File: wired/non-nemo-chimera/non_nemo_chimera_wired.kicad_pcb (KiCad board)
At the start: 2 copper layers, 273.7 x 107 mm, 94 parts, among them X1 5.5mm, X10 5.5mm, X2 5.5mm, X3 5.5mm, X4 5.5mm, X5 5.5mm, X6 5.5mm, X7 5.5mm, X8 5.5mm, X9 5.5mm

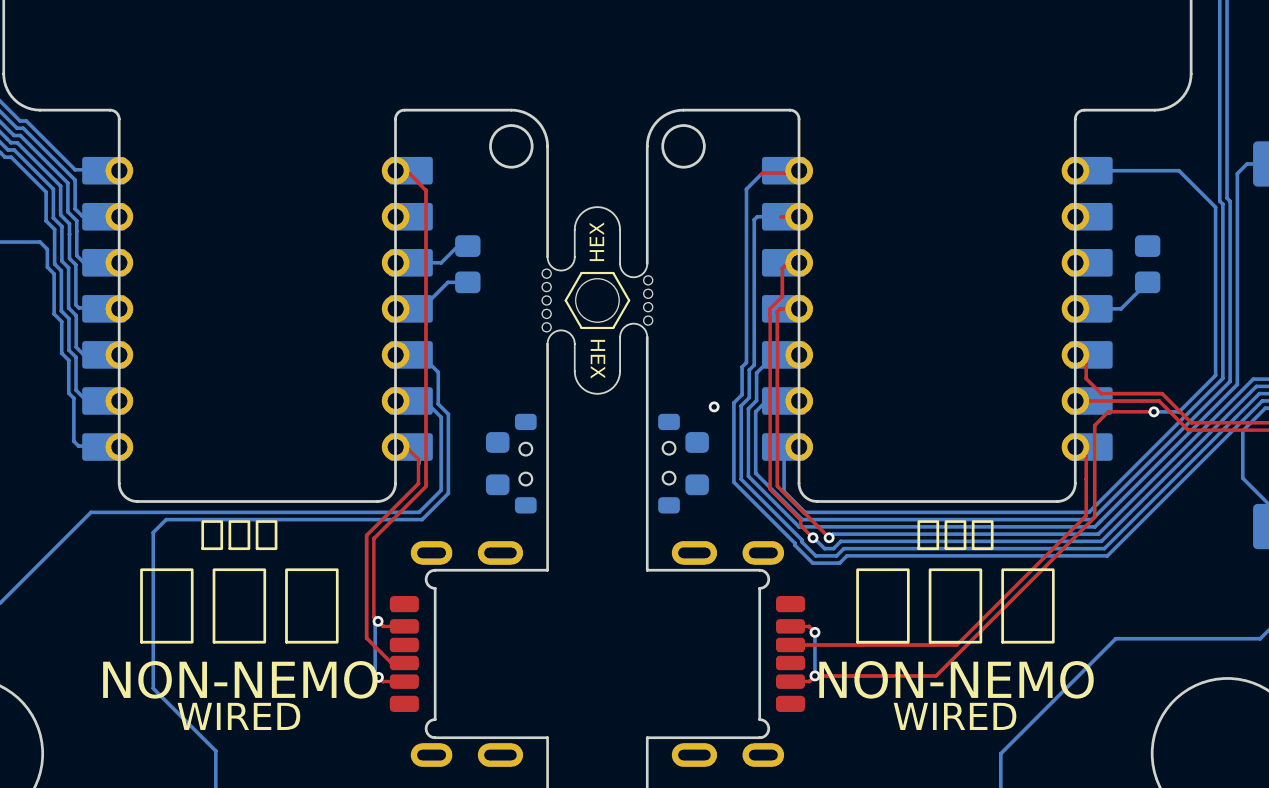
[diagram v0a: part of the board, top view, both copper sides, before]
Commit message: Chimera Wired + Case (#10)
* Updated cases for Chimera Wired

* updated README.md for Chimera Wired

* updated github workflow
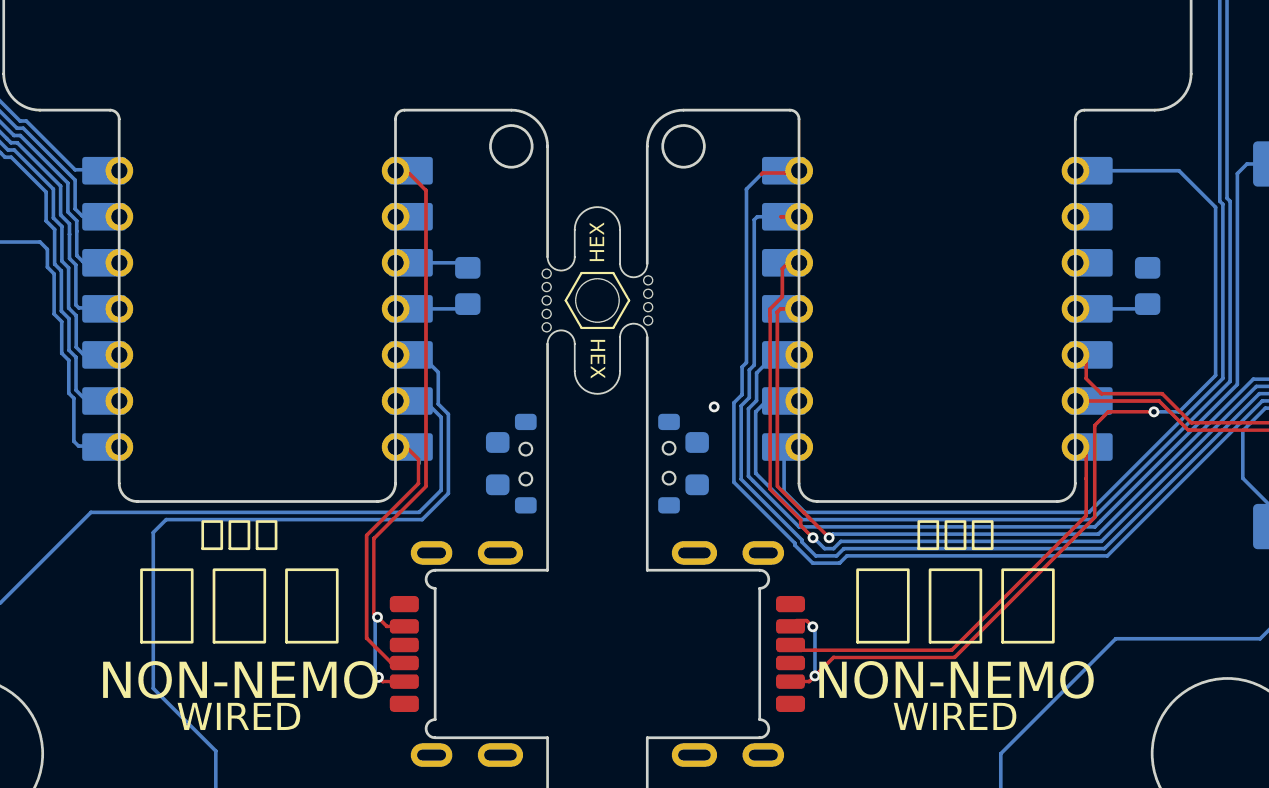
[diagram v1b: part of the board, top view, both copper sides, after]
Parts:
- moved R1 1.20 mm to (147.6, 84.2)
- moved R2 1.20 mm to (185.1, 84.2)
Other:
- board text added: "Non Nemo 0.2.1"
- board text removed: "Non Nemo 0.2.0"
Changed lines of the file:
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@@
 	(paper "A3")
 	(title_block
-		(title "Non Nemo Chimera")
-		(date "2025-04-09")
-		(rev "0.2.0")
+		(title "Non Nemo Chimera Wired")
+		(date "2025-04-21")
+		(rev "0.2.1")
 		(company "Allen Choi")
 	)
@@
 	(footprint "TB2086_SMD:R_0805_2012Metric_Pad1.20x1.40mm_HandSolder"
 		(layer "B.Cu")
-		(at 147.6 83 90)
+		(at 147.6 84.2 90)
 		(descr "Resistor SMD 0805 (2012 Metric), square (rectangular) end terminal, IPC_7351 nominal with elongated pad for handsoldering. (Body size source: IPC-SM-782 page 72, https://www.pcb-3d.com/wordpress/wp-content/uploads/ipc-sm-782a_amendment_1_and_2.pdf), generated with kicad-footprint-generator")
 		(tags "resistor handsolder")
@@
 	(footprint "TB2086_SMD:R_0805_2012Metric_Pad1.20x1.40mm_HandSolder"
 		(layer "B.Cu")
-		(at 185.1 83 90)
+		(at 185.1 84.2 90)
 		(descr "Resistor SMD 0805 (2012 Metric), square (rectangular) end terminal, IPC_7351 nominal with elongated pad for handsoldering. (Body size source: IPC-SM-782 page 72, https://www.pcb-3d.com/wordpress/wp-content/uploads/ipc-sm-782a_amendment_1_and_2.pdf), generated with kicad-footprint-generator")
 		(tags "resistor handsolder")
@@
 		(fp_arc
 			(start 8.129769 10.962553)
-			(mid 7.776218 10.816103)
+			(mid 7.776217 10.816099)
 			(end 7.629769 10.462553)
 			(stroke
@@
 		(fp_arc
 			(start 8.129769 10.962553)
-			(mid 7.776218 10.816103)
+			(mid 7.776217 10.816099)
 			(end 7.629769 10.462553)
 			(stroke
@@
 	)
 	(gr_text "Powered By Ergogen"
-		(at 173.5 109 0)
+		(at 174.5 103.5 0)
 		(layer "B.SilkS")
 		(effects
@@
 		)
 	)
-	(gr_text "Non Nemo 0.2.0"
+	(gr_text "Non Nemo 0.2.1"
 		(at 259.5 109.5 0)
 		(layer "B.SilkS")
@@
 		)
 	)
-	(gr_text "Non Nemo 0.2.0"
+	(gr_text "Non Nemo 0.2.1"
 		(at 50 109.5 0)
 		(layer "B.SilkS")
@@
 	)
 	(gr_text "Powered By Ergogen"
-		(at 136 109 0)
+		(at 135 103.5 0)
 		(layer "B.SilkS")
 		(effects
@@
 	)
 	(segment
-		(start 166.44 106.02)
-		(end 165.4 106.02)
+		(start 182.937007 91.142993)
+		(end 182.182 91.898)
 		(width 0.2)
 		(layer "F.Cu")
@@
 	)
 	(segment
-		(start 142.42 98.125686)
-		(end 145.29 95.255686)
+		(start 145.29 95.255686)
+		(end 145.29 78.923193)
 		(width 0.2)
 		(layer "F.Cu")
@@
 	)
 	(segment
-		(start 185.447892 91.142993)
-		(end 182.937007 91.142993)
+		(start 143.13 102.98)
+		(end 144.1 102.98)
+		(width 0.2)
+		(layer "F.Cu")
+		(net 58)
+	)
+	(segment
+		(start 174.455686 104.69)
+		(end 167.77 104.69)
+		(width 0.2)
+		(layer "F.Cu")
+		(net 58)
+	)
+	(segment
+		(start 166.44 106.02)
+		(end 165.4 106.02)
 		(width 0.2)
 		(layer "F.Cu")
@@
 	)
 	(segment
-		(start 182.937007 91.142993)
-		(end 182.182 91.898)
+		(start 165.72 102.66)
+		(end 165.4 102.98)
 		(width 0.2)
 		(layer "F.Cu")
@@
 	)
 	(segment
-		(start 173.435686 105.71)
-		(end 166.75 105.71)
+		(start 142.42 102.27)
+		(end 142.42 98.125686)
 		(width 0.2)
 		(layer "F.Cu")
@@
 	)
 	(segment
-		(start 142.65 102.7)
-		(end 142.42 102.47)
+		(start 166.63 103)
+		(end 166.29 102.66)
 		(width 0.2)
 		(layer "F.Cu")
@@
 	)
 	(segment
-		(start 166.42 102.98)
-		(end 165.4 102.98)
+		(start 142.62 102.47)
+		(end 143.13 102.98)
 		(width 0.2)
 		(layer "F.Cu")
@@
 	)
 	(segment
-		(start 142.42 102.47)
-		(end 142.42 98.125686)
+		(start 142.42 98.125686)
+		(end 145.29 95.255686)
 		(width 0.2)
 		(layer "F.Cu")
@@
 	)
 	(segment
-		(start 142.93 102.98)
-		(end 144.1 102.98)
+		(start 167.77 104.69)
+		(end 166.75 105.71)
 		(width 0.2)
 		(layer "F.Cu")
@@
 	(segment
 		(start 182.182 96.963686)
-		(end 173.435686 105.71)
+		(end 174.455686 104.69)
 		(width 0.2)
 		(layer "F.Cu")
@@
 	)
 	(segment
-		(start 166.75 103.31)
-		(end 166.42 102.98)
+		(start 142.62 102.47)
+		(end 142.42 102.27)
 		(width 0.2)
 		(layer "F.Cu")
@@
 	)
 	(segment
-		(start 142.65 102.7)
-		(end 142.93 102.98)
+		(start 166.75 105.71)
+		(end 166.44 106.02)
 		(width 0.2)
 		(layer "F.Cu")
@@
 	)
 	(segment
-		(start 166.75 105.71)
-		(end 166.44 106.02)
+		(start 142.67 105.79)
+		(end 142.9 106.02)
 		(width 0.2)
 		(layer "F.Cu")
@@
 	)
 	(segment
-		(start 142.67 105.79)
-		(end 142.9 106.02)
+		(start 166.29 102.66)
+		(end 165.72 102.66)
 		(width 0.2)
 		(layer "F.Cu")
@@
 	)
 	(segment
-		(start 145.29 95.255686)
-		(end 145.29 78.923193)
+		(start 185.447892 91.142993)
+		(end 182.937007 91.142993)
 		(width 0.2)
 		(layer "F.Cu")
@@
 	)
 	(via
-		(at 166.75 103.31)
+		(at 166.63 103)
 		(size 0.6)
 		(drill 0.3)
@@
 	)
 	(via
-		(at 142.65 102.7)
+		(at 142.62 102.47)
 		(size 0.6)
 		(drill 0.3)
@@
 	)
 	(segment
-		(start 188.85 79.86)
-		(end 186.833 77.843)
+		(start 142.49 102.6)
+		(end 142.49 105.61)
 		(width 0.2)
 		(layer "B.Cu")
@@
 	)
 	(segment
-		(start 185.447892 91.142993)
-		(end 186.841321 91.142993)
+		(start 142.49 105.61)
+		(end 142.67 105.79)
 		(width 0.2)
 		(layer "B.Cu")
@@
 	)
 	(segment
-		(start 142.49 105.61)
-		(end 142.49 102.86)
+		(start 166.63 103)
+		(end 166.75 103.12)
 		(width 0.2)
 		(layer "B.Cu")
@@
 	)
 	(segment
-		(start 142.49 102.86)
-		(end 142.65 102.7)
+		(start 188.85 79.86)
+		(end 186.833 77.843)
 		(width 0.2)
 		(layer "B.Cu")
@@
 	)
 	(segment
-		(start 142.67 105.79)
-		(end 142.49 105.61)
+		(start 185.447892 91.142993)
+		(end 186.841321 91.142993)
 		(width 0.2)
 		(layer "B.Cu")
@@
 	)
 	(segment
-		(start 186.841321 91.142993)
-		(end 188.85 89.134314)
+		(start 142.62 102.47)
+		(end 142.49 102.6)
 		(width 0.2)
 		(layer "B.Cu")
@@
 	)
 	(segment
-		(start 166.75 103.31)
+		(start 166.75 103.12)
 		(end 166.75 105.71)
 		(width 0.2)
@@
 	)
 	(segment
-		(start 181.709996 96.870004)
-		(end 181.709996 94.840735)
+		(start 186.841321 91.142993)
+		(end 188.85 89.134314)
 		(width 0.2)
-		(layer "F.Cu")
-		(net 59)
+		(layer "B.Cu")
+		(net 58)
 	)
 	(segment
@@
 	)
 	(segment
-		(start 174.58 104)
+		(start 165.69 104.29)
+		(end 174.29 104.29)
+		(width 0.2)
+		(layer "F.Cu")
+		(net 59)
+	)
+	(segment
+		(start 174.29 104.29)
 		(end 181.709996 96.870004)
 		(width 0.2)
@@
 	(segment
 		(start 165.4 104)
-		(end 174.58 104)
+		(end 165.69 104.29)
+		(width 0.2)
+		(layer "F.Cu")
+		(net 59)
+	)
+	(segment
+		(start 181.709996 96.870004)
+		(end 181.709996 94.840735)
 		(width 0.2)
 		(layer "F.Cu")
@@
 	)
 	(segment
-		(start 183.637 85.463)
-		(end 185.1 84)
+		(start 184.837 85.463)
+		(end 185.1 85.2)
 		(width 0.2)
 		(layer "B.Cu")
@@
 	(segment
 		(start 181.955 85.463)
-		(end 183.637 85.463)
+		(end 184.837 85.463)
 		(width 0.2)
 		(layer "B.Cu")
@@
 	)
 	(segment
-		(start 146.51 84)
-		(end 147.6 84)
-		(width 0.2)
-		(layer "B.Cu")
-		(net 64)
-	)
-	(segment
-		(start 145.047 85.463)
-		(end 146.51 84)
+		(start 147.337 85.463)
+		(end 147.6 85.2)
 		(width 0.2)
 		(layer "B.Cu")
@@
 	(segment
 		(start 144.455 85.463)
-		(end 145.047 85.463)
+		(end 147.337 85.463)
 		(width 0.2)
 		(layer "B.Cu")
@@
 	)
 	(segment
-		(start 146.137 82.923)
-		(end 147.06 82)
-		(width 0.2)
-		(layer "B.Cu")
-		(net 65)
-	)
-	(segment
-		(start 147.06 82)
-		(end 147.6 82)
+		(start 144.455 82.923)
+		(end 147.323 82.923)
 		(width 0.2)
 		(layer "B.Cu")
@@
 	)
 	(segment
-		(start 144.455 82.923)
-		(end 146.137 82.923)
+		(start 147.323 82.923)
+		(end 147.6 83.2)
 		(width 0.2)
 		(layer "B.Cu")

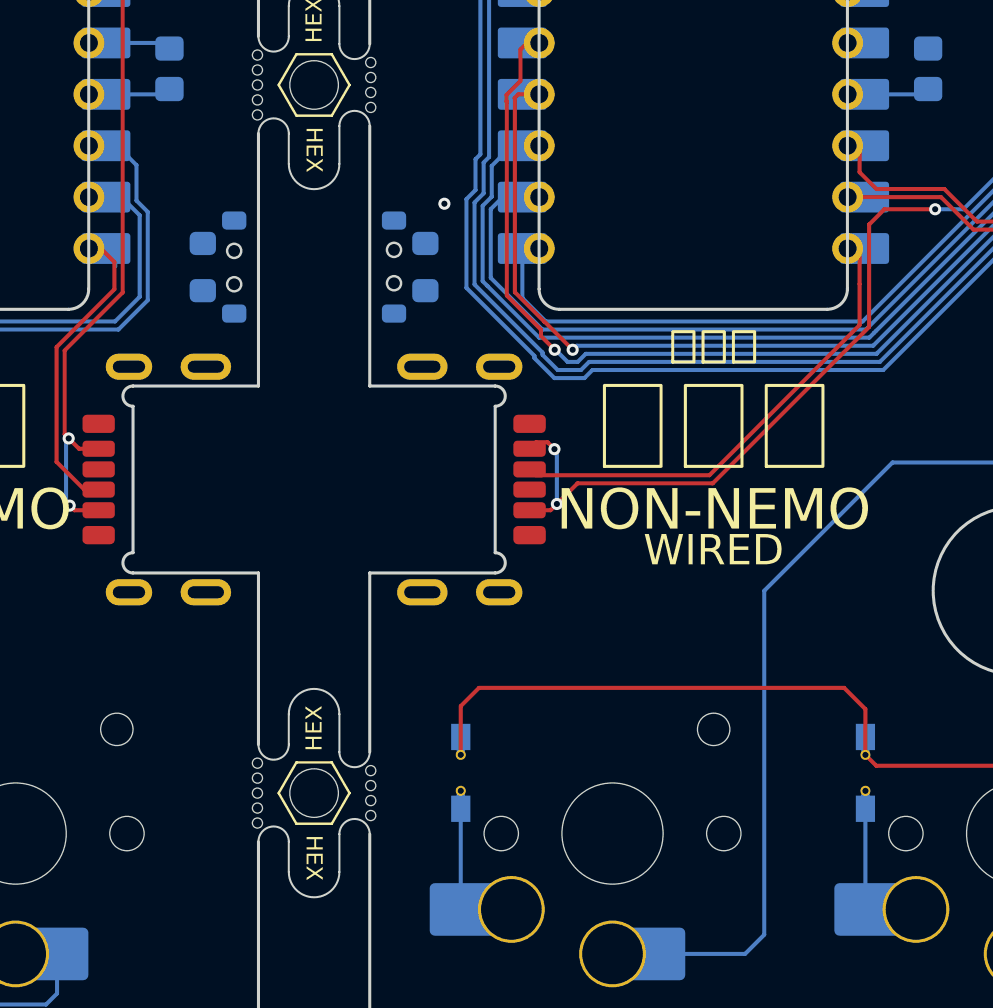
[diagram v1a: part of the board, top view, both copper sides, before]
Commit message: fixed Wired (#12)
* fixed Non Nemo Wired

* fixed ergogen for Wired
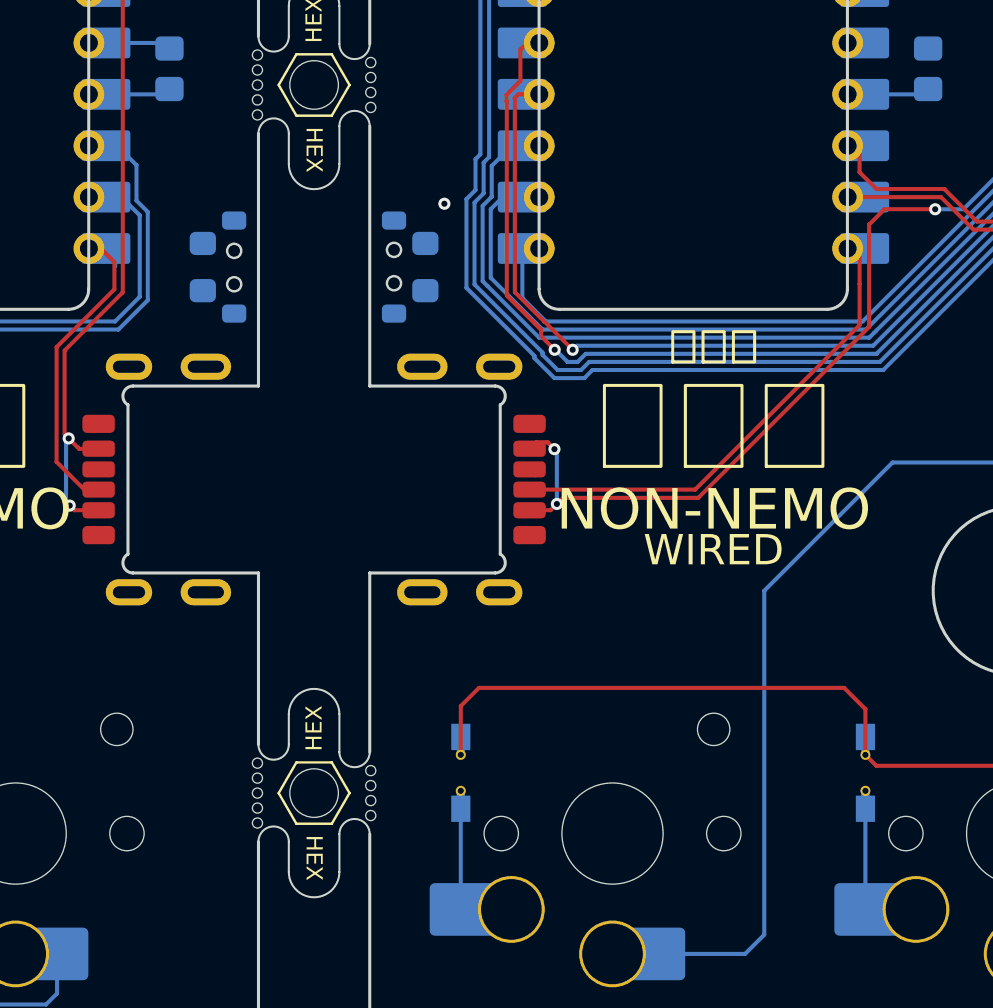
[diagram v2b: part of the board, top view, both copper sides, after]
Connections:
- USB2 pad A5: DATA_r -> unconnected-(USB2-CC1-PadA5)
- USB2 pad B5: unconnected-(USB2-CC2-PadB5) -> DATA_r
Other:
- board text added: "Non Nemo 0.2.2"
- board text removed: "B+"
- board text removed: "Non Nemo 0.2.1"
